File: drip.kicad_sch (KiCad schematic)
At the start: 97 parts, among them J1 ISP, J2 2xAA Battery Holder, Q1 2n2907, Q2 2n2907, Q3 2n2907, Q4 2n2907, Q5 2n2907, Q6 2n2907, Q7 2n2907, Q8 2n2907, Q9 2n2222, SW1 Bin, SW10 Recall, SW11 D, SW12 A, SW13 7, SW14 4, SW15 1, SW16 0, SW17 Hex, SW18 E, SW19 B, SW2 Store, SW20 8, SW21 5, SW22 2, SW23 Decimal, SW24 Oct, SW25 F, SW26 C, SW27 9, SW28 6, SW29 3, SW3 Shift, SW30 +/-, SW31 Clear, SW32 K, SW33 Div, SW34 Mul, SW35 Minus, SW36 Plus, SW37 Enter, SW4 1'sCompl, SW5 Or, SW6 And, SW7 Xor, SW8 Clear Entry, SW9 Dec, U1 74HC138, U2 5641AS-4Digit-7Segment, U3 5641AS-4Digit-7Segment, U4 MSP430G2553IN20, U5 74HC251, U6 74HC138, U7 74HC595, U8 XC6372A331PR-G

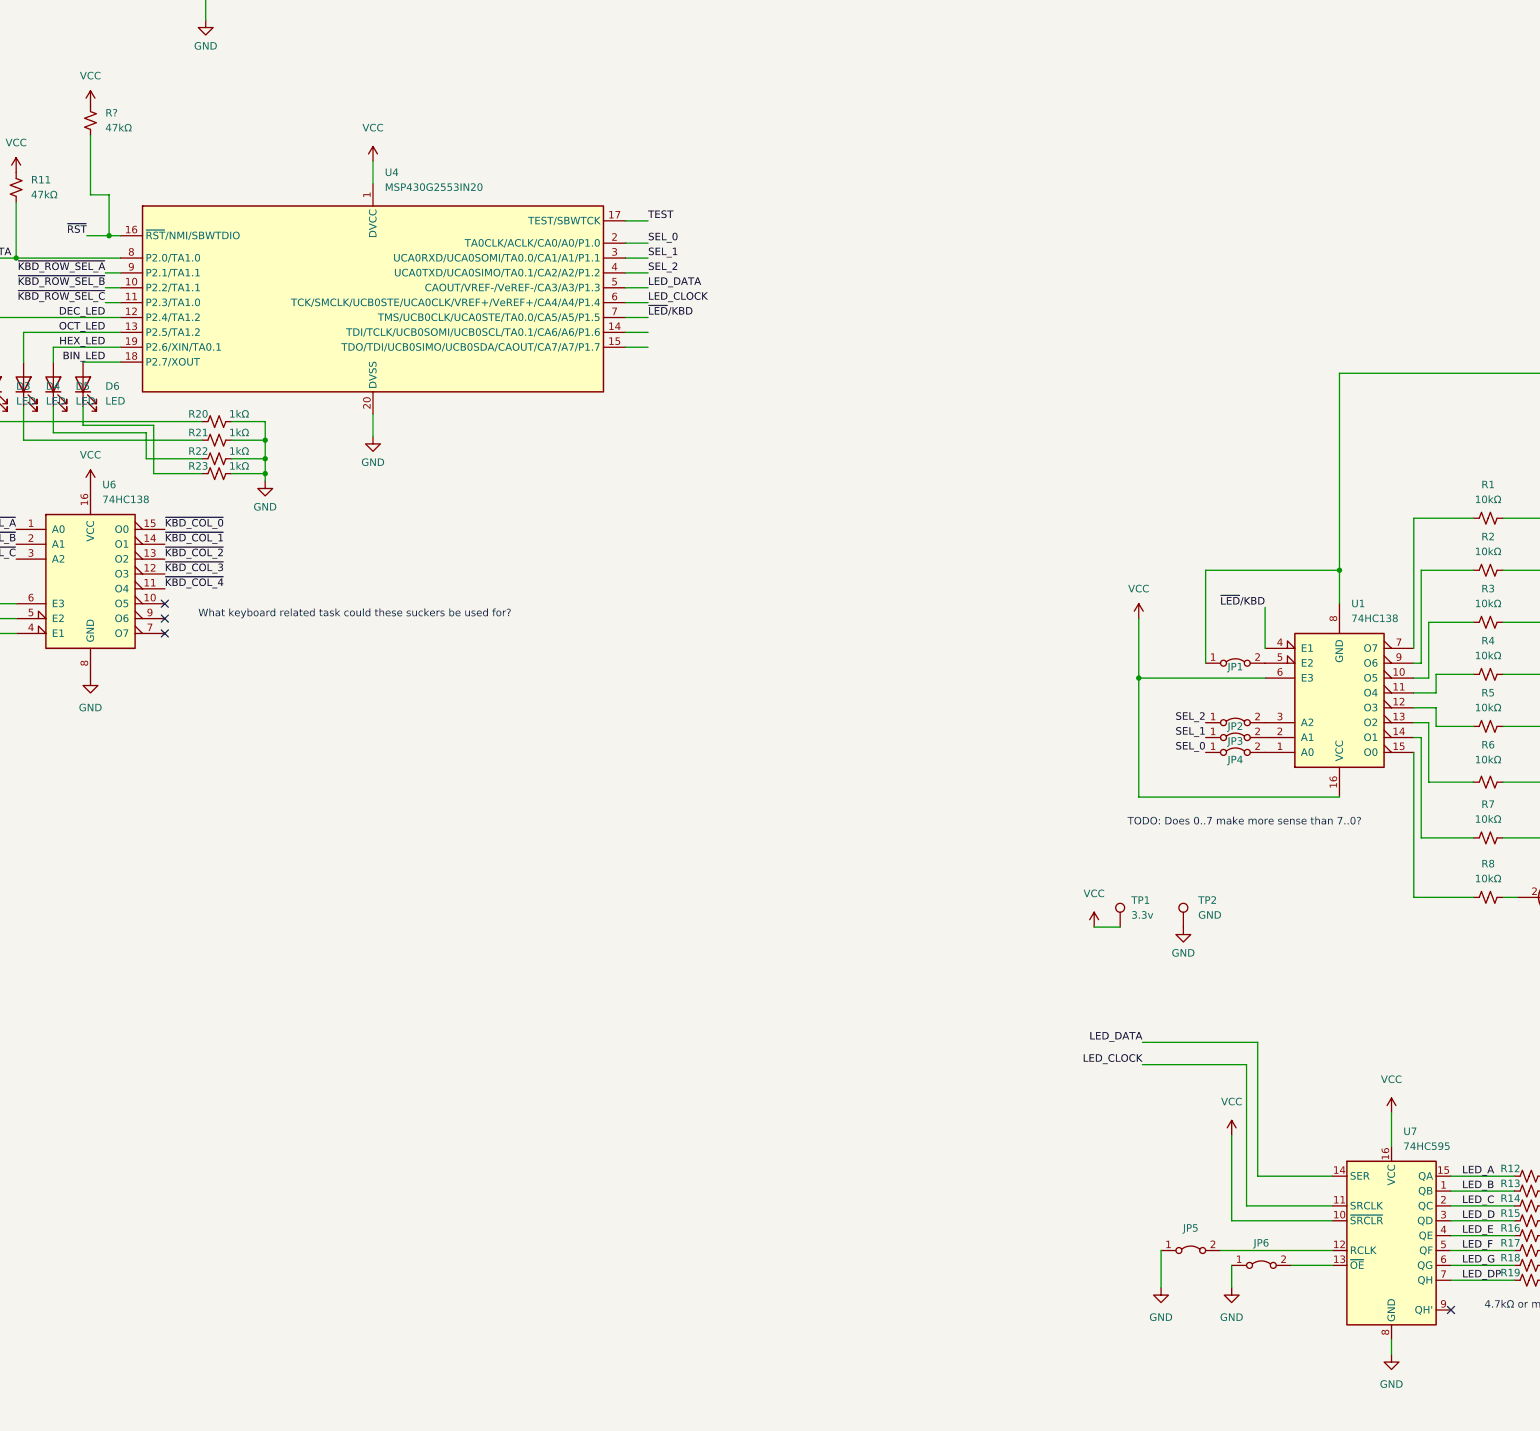
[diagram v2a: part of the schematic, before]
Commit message: 7-segment working with latch bodge
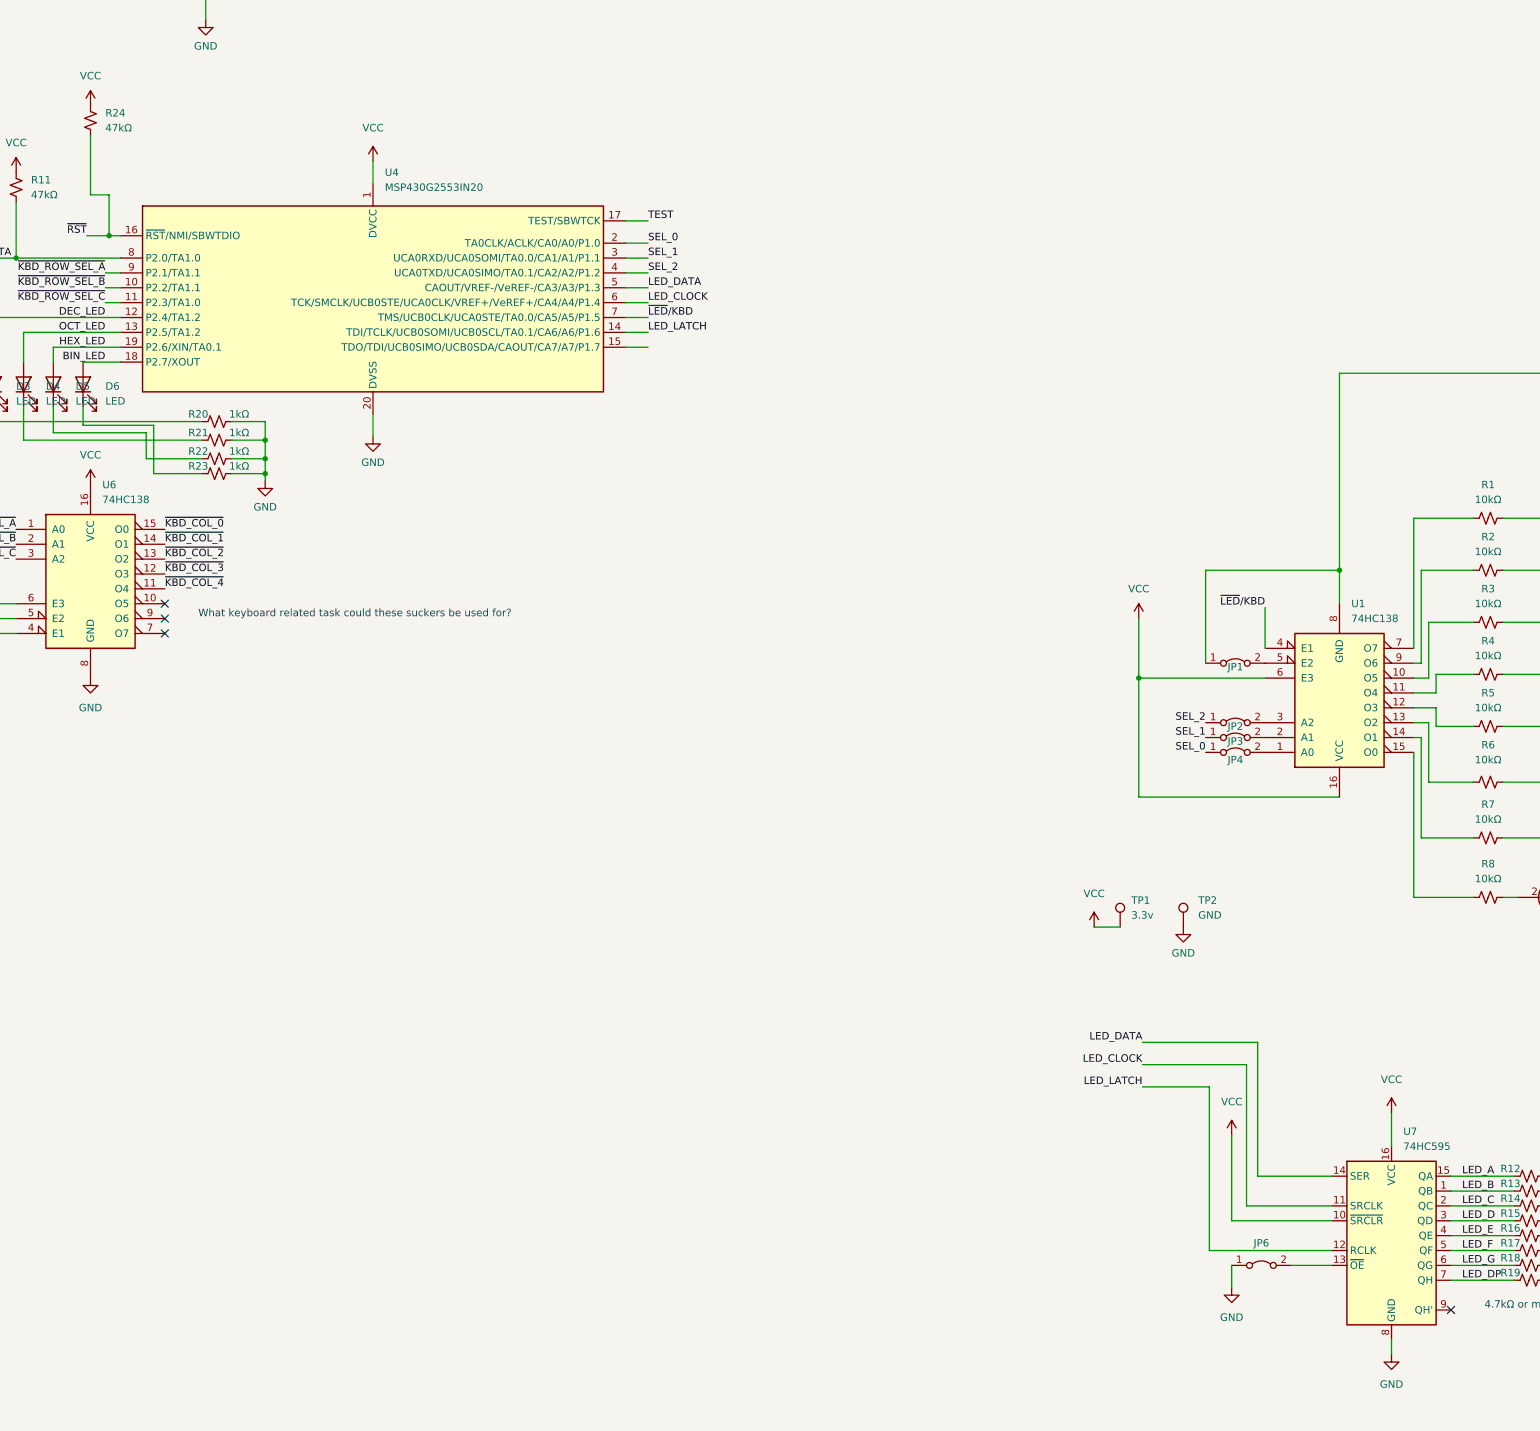
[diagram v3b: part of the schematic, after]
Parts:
- removed JP5: Jumper_2_Bridged, Jumper:SolderJumper-2_P1.3mm_Bridged2Bar_RoundedPad1.0x1.5mm, symbol Jumper:Jumper_2_Bridged
- gave numbers to parts that had none: 1
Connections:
- net LED_LATCH: now reaches U4.14 (TDI/TCLK/UCB0SOMI/UCB0SCL/TA0.1/CA6/A6/P1.6)
- net LED_LATCH: now also U7.12 (RCLK)
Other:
- note removed: "TODO: Does 0..7 make more sense than 7..0?"
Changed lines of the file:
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@@
     (stroke (width 0) (type default) (color 0 0 0 0))
   )
-  (wire (pts (xy 330.2 351.79) (xy 330.2 358.14))
-    (stroke (width 0) (type default) (color 0 0 0 0))
-  )
   (wire (pts (xy 416.56 356.87) (xy 467.36 356.87))
     (stroke (width 0) (type default) (color 0 0 0 0))
@@
     (stroke (width 0) (type default) (color 0 0 0 0))
   )
+  (wire (pts (xy 338.455 351.79) (xy 338.455 323.85))
+    (stroke (width 0) (type default) (color 0 0 0 0))
+  )
   (wire (pts (xy 92.71 333.375) (xy 101.6 333.375))
     (stroke (width 0) (type default) (color 0 0 0 0))
@@
     (stroke (width 0) (type default) (color 0 0 0 0))
   )
+  (wire (pts (xy 338.455 323.85) (xy 327.025 323.85))
+    (stroke (width 0) (type default) (color 0 0 0 0))
+  )
   (wire (pts (xy 379.73 344.17) (xy 390.525 344.17))
     (stroke (width 0) (type default) (color 0 0 0 0))
@@
     (stroke (width 0) (type default) (color 0 0 0 0))
   )
-  (wire (pts (xy 340.36 351.79) (xy 359.41 351.79))
+  (wire (pts (xy 338.455 351.79) (xy 359.41 351.79))
     (stroke (width 0) (type default) (color 0 0 0 0))
   )
@@
     (effects (font (size 1.27 1.27)) (justify left bottom))
   )
-  (text "TODO: Does 0..7 make more sense than 7..0?" (at 324.485 279.4 0)
-    (effects (font (size 1.27 1.27)) (justify left bottom))
-  )
   (text "Keyboard Row Selector" (at 121.92 217.805 90)
     (effects (font (size 1.27 1.27)) (justify left bottom))
@@
     (effects (font (size 1.27 1.27)) (justify right bottom))
   )
+  (label "LED_LATCH" (at 327.025 323.85 180)
+    (effects (font (size 1.27 1.27)) (justify right bottom))
+  )
   (label "LED{slash}~{KBD}" (at 76.2 215.265 180)
     (effects (font (size 1.27 1.27)) (justify right bottom))
@@
     (effects (font (size 1.27 1.27)) (justify left bottom))
   )
+  (label "LED_LATCH" (at 242.57 194.945 0)
+    (effects (font (size 1.27 1.27)) (justify left bottom))
+  )
   (label "SEL_0" (at 337.82 266.7 180)
     (effects (font (size 1.27 1.27)) (justify right bottom))
@@
     (pin "2")
   )
-  (symbol (lib_id "power:GND") (at 330.2 358.14 0) (unit 1)
-    (in_bom yes) (on_board yes) (fields_autoplaced)
-    (property "Reference" "#PWR0110" (id 0) (at 330.2 364.49 0)
-      (effects (font (size 1.27 1.27)) hide)
-    )
-    (property "Value" "GND" (id 1) (at 330.2 363.22 0))
-    (property "Footprint" "" (id 2) (at 330.2 358.14 0)
-      (effects (font (size 1.27 1.27)) hide)
-    )
-    (property "Datasheet" "" (id 3) (at 330.2 358.14 0)
-      (effects (font (size 1.27 1.27)) hide)
-    )
-    (pin "1")
-  )
   (symbol (lib_id "power:VCC") (at 326.39 243.84 0) (unit 1)
     (in_bom yes) (on_board yes) (fields_autoplaced)
@@
   (symbol (lib_id "power:VCC") (at 147.32 156.21 0) (unit 1)
     (in_bom yes) (on_board yes) (fields_autoplaced)
-    (property "Reference" "#PWR?" (id 0) (at 147.32 160.02 0)
+    (property "Reference" "#PWR0122" (id 0) (at 147.32 160.02 0)
       (effects (font (size 1.27 1.27)) hide)
     )
@@
     (pin "1")
   )
-  (symbol (lib_id "Jumper:Jumper_2_Bridged") (at 335.28 351.79 0) (unit 1)
-    (in_bom yes) (on_board yes) (fields_autoplaced)
-    (property "Reference" "JP5" (id 0) (at 335.28 347.98 0))
-    (property "Value" "Jumper_2_Bridged" (id 1) (at 335.28 348.615 0)
-      (effects (font (size 1.27 1.27)) hide)
-    )
-    (property "Footprint" "Jumper:SolderJumper-2_P1.3mm_Bridged2Bar_RoundedPad1.0x1.5mm" (id 2) (at 335.28 351.79 0)
-      (effects (font (size 1.27 1.27)) hide)
-    )
-    (property "Datasheet" "~" (id 3) (at 335.28 351.79 0)
-      (effects (font (size 1.27 1.27)) hide)
-    )
-    (pin "1")
-    (pin "2")
-  )
   (symbol (lib_id "power:GND") (at 334.01 296.545 0) (unit 1)
     (in_bom yes) (on_board yes) (fields_autoplaced)
@@
   (symbol (lib_id "Device:R_Small_US") (at 147.32 158.75 0) (unit 1)
     (in_bom yes) (on_board yes) (fields_autoplaced)
-    (property "Reference" "R?" (id 0) (at 149.86 157.4799 0)
+    (property "Reference" "R24" (id 0) (at 149.86 157.4799 0)
       (effects (font (size 1.27 1.27)) (justify left))
     )
@@
       (reference "#PWR0109") (unit 1) (value "VCC") (footprint "")
     )
-    (path "/34823454-37e7-44f6-8ed8-7af3e991d2e7"
-      (reference "#PWR0110") (unit 1) (value "GND") (footprint "")
-    )
     (path "/c425aaae-74ff-4690-b6c2-dbf4091ccf90"
       (reference "#PWR0111") (unit 1) (value "VCC") (footprint "")
@@
     )
     (path "/5fe5395c-78d6-40cf-b4c7-813897577b4a"
-      (reference "#PWR?") (unit 1) (value "VCC") (footprint "")
+      (reference "#PWR0122") (unit 1) (value "VCC") (footprint "")
     )
     (path "/f2caa468-bb79-49cc-b0cf-a4c553ec891c"
@@
       (reference "JP4") (unit 1) (value "Jumper_2_Bridged") (footprint "Jumper:SolderJumper-2_P1.3mm_Bridged2Bar_RoundedPad1.0x1.5mm")
     )
-    (path "/61044d30-1770-4c3d-b97d-7db5b532ad09"
-      (reference "JP5") (unit 1) (value "Jumper_2_Bridged") (footprint "Jumper:SolderJumper-2_P1.3mm_Bridged2Bar_RoundedPad1.0x1.5mm")
-    )
     (path "/0445bf15-da07-48c0-a8de-26862fcf9018"
       (reference "JP6") (unit 1) (value "Jumper_2_Bridged") (footprint "Jumper:SolderJumper-2_P1.3mm_Bridged2Bar_RoundedPad1.0x1.5mm")
@@
     )
     (path "/c89464ff-21e6-4876-b3fa-6ec0b5c531f1"
-      (reference "R?") (unit 1) (value "47kΩ") (footprint "Resistor_THT:R_Axial_DIN0207_L6.3mm_D2.5mm_P10.16mm_Horizontal")
+      (reference "R24") (unit 1) (value "47kΩ") (footprint "Resistor_THT:R_Axial_DIN0207_L6.3mm_D2.5mm_P10.16mm_Horizontal")
     )
     (path "/f2abe8e1-ca83-4046-8fbf-377cee622491"

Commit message: Tinkering
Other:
- note added: "10kΩ is probably too much (dim when oscillating)"
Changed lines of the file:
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@@
     (stroke (width 0) (type default) (color 0 0 0 0))
+  )
+  (text "10kΩ is probably too much (dim when oscillating)" (at 385.445 364.49 0)
+    (effects (font (size 1.27 1.27)) (justify left bottom))
   )
   (text "TODO: Some kind of power switch?" (at 91.44 50.8 0)

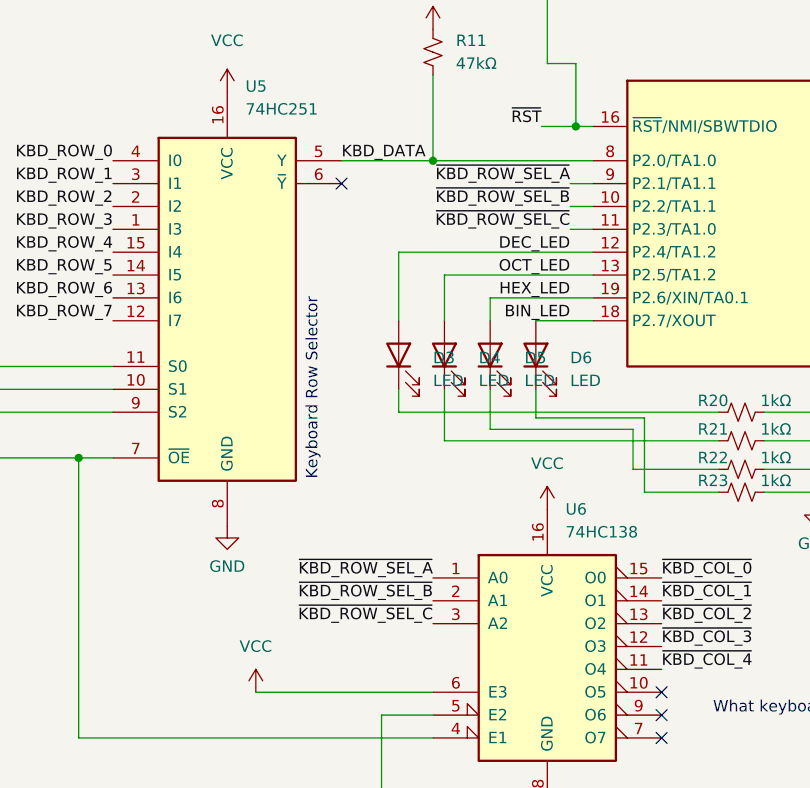
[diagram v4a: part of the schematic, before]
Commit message: Working keyboard scanner, I think
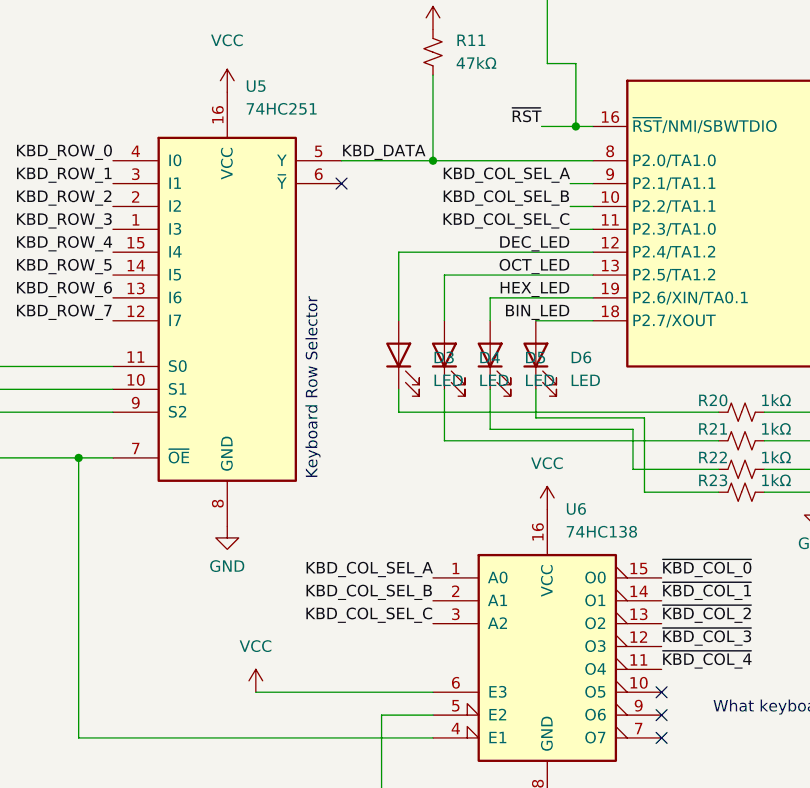
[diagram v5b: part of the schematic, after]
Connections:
- net ~{KBD_ROW_SEL_A} renamed KBD_COL_SEL_A
- net ~{KBD_ROW_SEL_B} renamed KBD_COL_SEL_B
- net ~{KBD_ROW_SEL_C} renamed KBD_COL_SEL_C
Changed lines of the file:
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@@
     (effects (font (size 1.27 1.27)) (justify right bottom))
   )
-  (label "~{KBD_ROW_SEL_B}" (at 134.62 231.14 180)
+  (label "KBD_COL_SEL_B" (at 134.62 231.14 180)
     (effects (font (size 1.27 1.27)) (justify right bottom))
   )
@@
     (effects (font (size 1.27 1.27)) (justify right bottom))
   )
-  (label "~{KBD_ROW_SEL_A}" (at 134.62 228.6 180)
+  (label "KBD_COL_SEL_A" (at 134.62 228.6 180)
     (effects (font (size 1.27 1.27)) (justify right bottom))
   )
@@
     (effects (font (size 1.27 1.27)) (justify right bottom))
   )
-  (label "~{KBD_ROW_SEL_C}" (at 134.62 233.68 180)
+  (label "KBD_COL_SEL_C" (at 134.62 233.68 180)
     (effects (font (size 1.27 1.27)) (justify right bottom))
   )
@@
     (effects (font (size 1.27 1.27)) (justify right bottom))
   )
-  (label "~{KBD_ROW_SEL_A}" (at 149.86 184.785 180)
+  (label "KBD_COL_SEL_A" (at 149.86 184.785 180)
     (effects (font (size 1.27 1.27)) (justify right bottom))
   )
@@
     (effects (font (size 1.27 1.27)) (justify right bottom))
   )
-  (label "~{KBD_ROW_SEL_B}" (at 149.86 187.325 180)
+  (label "KBD_COL_SEL_B" (at 149.86 187.325 180)
     (effects (font (size 1.27 1.27)) (justify right bottom))
   )
@@
     (effects (font (size 1.27 1.27)) (justify right bottom))
   )
-  (label "~{KBD_ROW_SEL_C}" (at 149.86 189.865 180)
+  (label "KBD_COL_SEL_C" (at 149.86 189.865 180)
     (effects (font (size 1.27 1.27)) (justify right bottom))
   )
